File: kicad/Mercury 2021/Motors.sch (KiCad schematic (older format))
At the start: 13 parts

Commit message: Updated new board
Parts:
- removed U? (x4): MDD10A, symbol Mercury:MDD10A
- removed U? (x2): PCA9685, symbol Mercury:PCA9685
- added J22: Conn_02x03_Counter_Clockwise, symbol Connector_Generic:Conn_02x03_Counter_Clockwise
- added J23, J24: Conn_01x02_Female, symbol Connector:Conn_01x02_Female
- added J25: Conn_01x06_Female, symbol Connector:Conn_01x06_Female
- added J26, J27, J29: Conn_01x05_Female, symbol Connector:Conn_01x05_Female
- added J28: Conn_01x03_Female, symbol Connector:Conn_01x03_Female
- added unit 4 of U12
- added unit 5 of U12
- U11, U13: renamed from U?; value MDD10A -> PCA9685; footprint (none) -> Connector_PinHeader_2.54mm:PinHeader_1x05_P2.54mm_Vertical
- U12: renamed from U?; footprint (none) -> Connector_PinHeader_2.54mm:PinHeader_1x06_P2.54mm_Vertical
- gave numbers to parts that had none: 1
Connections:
- net LM_GND: now also U13.1 (B-)
- net RM_GND: now also U11.1 (B-)
- net RM_VIN: now reaches U11.2 (B+)
- net LM_VIN: now reaches U13.2 (B+)
- net Servo_VIN: now reaches U12.1 (V+)
- net Servo_GND: now reaches U12.2 (GND)
- net Pi_3v3: now reaches J15.1 (3V3)
- net Pi_3v3: now also J15.17 (3V3), J26.4 (Pin_4), J26.5 (Pin_5)
- net Pi_GPIO15: now reaches J15.10 (GPIO15/RXD)
- net Pi_GPIO15: now also J23.1 (Pin_1)
- net Pi_GPIO17: now reaches J15.11 (GPIO17)
- net Pi_GPIO17: now also J24.1 (Pin_1)
- net Pi_GPIO27: now reaches J15.13 (GPIO27)
- net Pi_GPIO27: now also J25.1 (Pin_1)
- net Servo_GND_GND: now reaches J15.14 (GND)
- net Pi_GPIO22: now reaches J15.15 (GPIO22)
- net Pi_GPIO22: now also J25.6 (Pin_6)
- net Pi_GPIO23: now reaches J15.16 (GPIO23)
- net Pi_GPIO23: now also J25.5 (Pin_5)
- net Pi_GPIO24: now reaches J15.18 (GPIO24)
- net Pi_GPIO24: now also J25.4 (Pin_4)
- net Pi_GPIO10: now reaches J15.19 (MOSI0/GPIO10)
- net Pi_GPIO10: now also J29.4 (Pin_4)
- net Pi_5v: now reaches J15.2 (5V)
- net Pi_5v: now also J15.4 (5V), J26.1 (Pin_1), J26.2 (Pin_2)
- net Pi_GND: now reaches J15.20 (GND)
- net Pi_GND: now also J15.25 (GND), J15.30 (GND), J15.34 (GND), J15.39 (GND), J27.1 (Pin_1), J27.2 (Pin_2), J27.3 (Pin_3), J27.4 (Pin_4), J27.5 (Pin_5)
- net Pi_GPIO09: now reaches J15.21 (MISO0/GPIO9)
- net Pi_GPIO09: now also J29.3 (Pin_3)
- net Pi_GPIO25: now reaches J15.22 (GPIO25)
- net Pi_GPIO25: now also J25.3 (Pin_3)
- net Pi_GPIO11: now reaches J15.23 (SCLK0/GPIO11)
- net Pi_GPIO11: now also J29.5 (Pin_5)
- net Pi_GPIO08: now reaches J15.24 (~CE0~/GPIO8)
- net Pi_GPIO08: now also J29.2 (Pin_2)
- net Pi_GPIO07: now reaches J15.26 (~CE1~/GPIO7)
- net Pi_GPIO07: now also J29.1 (Pin_1)
- net Pi_GPIO00: now reaches J15.27 (ID_SD/GPIO0)
- net Pi_GPIO00: now also J28.1 (Pin_1)
- net Pi_GPIO01: now reaches J15.28 (ID_SC/GPIO1)
- net Pi_GPIO01: now also J28.2 (Pin_2)
- net Servo_SDA: now reaches J15.3 (SDA/GPIO2)
- net Servo_SDA: now also U12.4 (SDA)
- net Pi_GPIO16: now reaches J15.36 (GPIO16)
- net Pi_GPIO16: now also J24.2 (Pin_2)
- net Pi_GPIO26: now reaches J15.37 (GPIO26)
- net Pi_GPIO26: now also J25.2 (Pin_2)
- net Servo_SCL: now reaches J15.5 (SCL/GPIO3)
- net Servo_SCL: now also U12.3 (SCL)
- net Pi_GPIO04: now reaches J15.7 (GCLK0/GPIO4)
- net Pi_GPIO04: now also J28.3 (Pin_3)
- net Pi_GPIO14: now reaches J15.8 (GPIO14/TXD)
- net Pi_GPIO14: now also J23.2 (Pin_2)
- net Servo_CTL_GND: now reaches U12.1 (GND)
- net Servo_OE: now reaches U12.2 (OE)
- net Serco_VCC: now reaches U12.5 (VCC)
- net Servo_V+: now reaches U12.6 (V+)
- new net: J22.1 (Pin_1), U12.1 (PWM_0)
- new net: J22.2 (Pin_2), U12.2 (V+)
- new net: J22.3 (Pin_3), U12.3 (GND)
- new net: J22.6 (Pin_6), U12.1 (PWM_1)
- new net: J22.5 (Pin_5), U12.2 (V+)
- new net: J22.4 (Pin_4), U12.3 (GND)
- no-connect marks 0 -> 4
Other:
- moved on the sheet: U11C, U12C, U13C

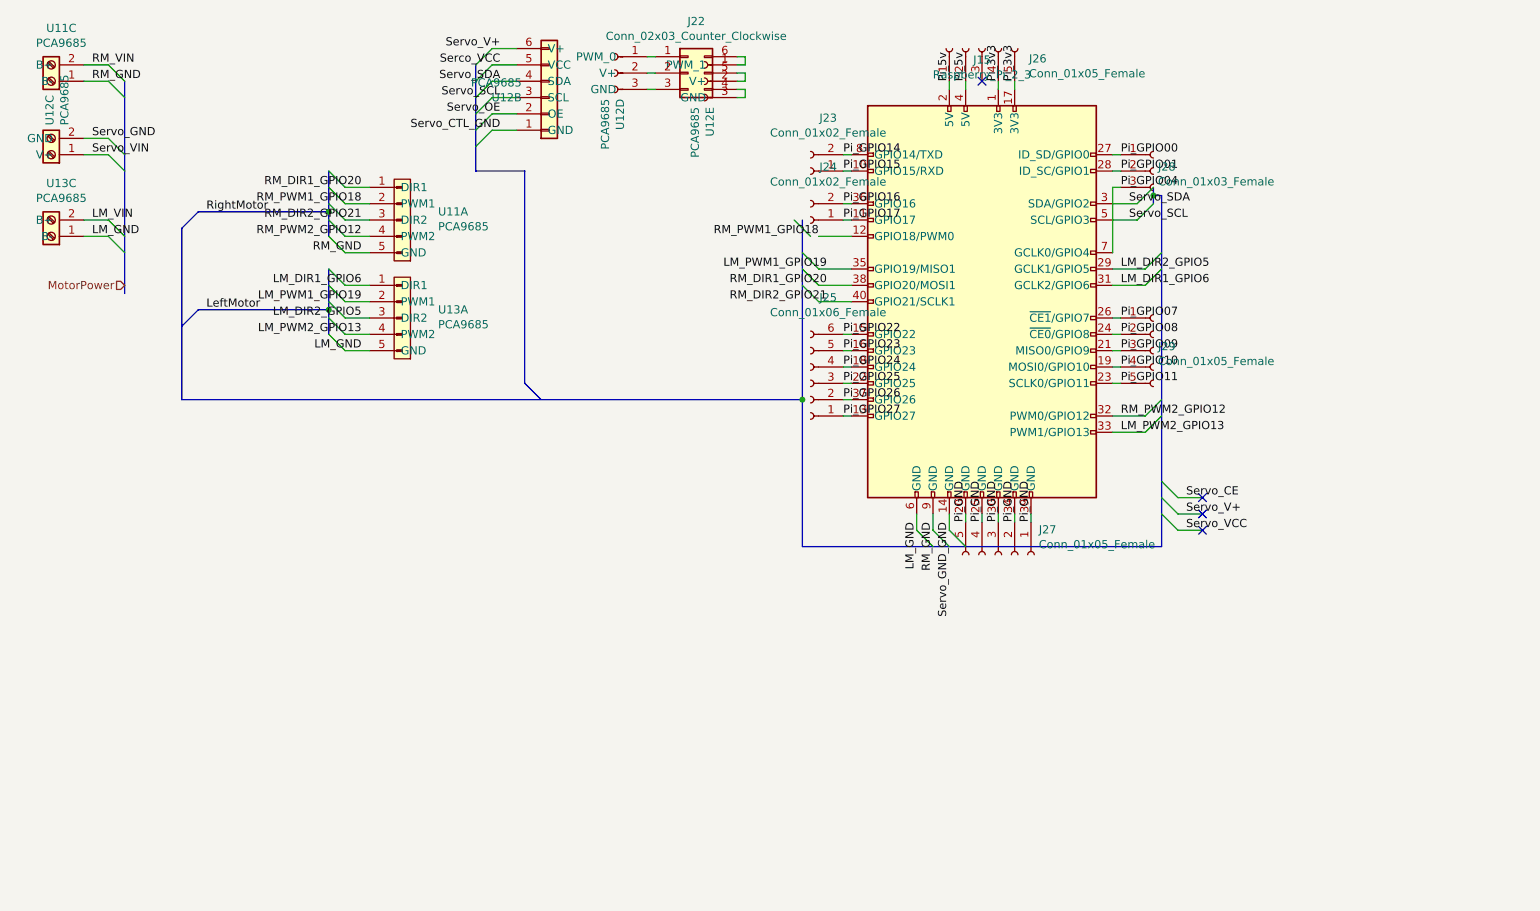
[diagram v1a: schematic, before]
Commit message: Updated the new PCB (lots of notes)
- added net
- changed symbols
- added footprints
- added ability to put the pi -> arduino cable through the board
- fixed global labels
- named connectors
- started adding things to title block

Notes:
- footprints for some parts were chosen at random, connectors need to be chosen on digikey
-- connectors for ribbon cables
-- USB connectors
-- screw terminals
- for these, the footprints may be wrong, so we need to make sure the connectors for them are spaced right
-- arduino
-- servo controller
-- PWM controller
- Board is unorganized, cluttered, and unusable, needs to be managed. considerations:
-- Pins carrying power and data should be separated by distance or GND
-- able to access connectors (not blocked by other things)
- Finish adding things to the title blocks and the PCB silkscreen
-- names or members
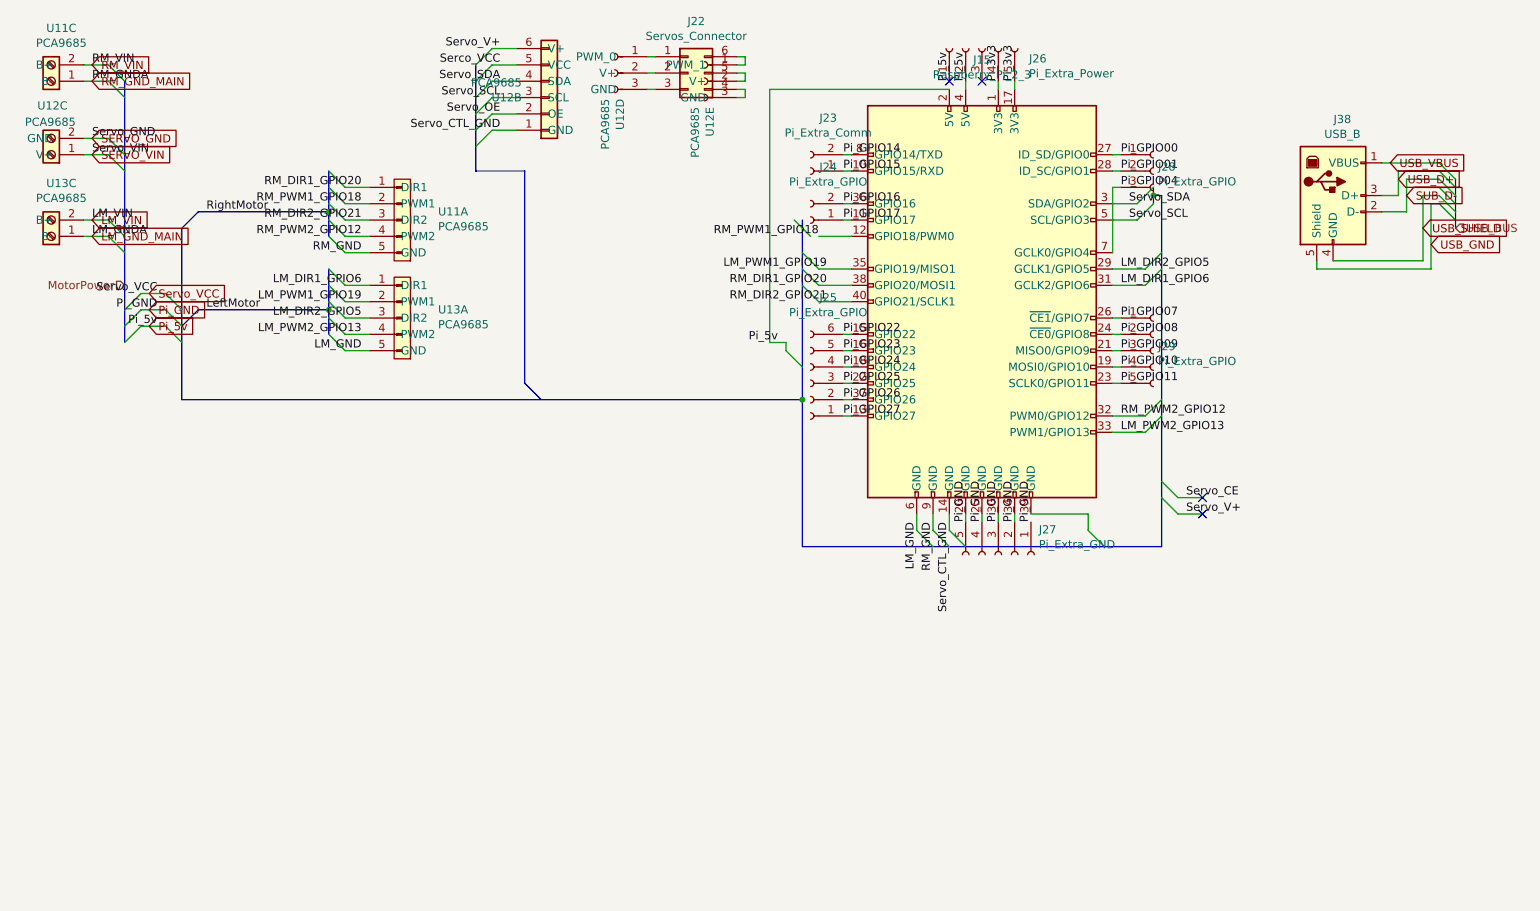
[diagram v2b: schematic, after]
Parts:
- added J38: USB_B, Connector_USB:USB_B_TE_5787834_Vertical, symbol Connector:USB_B
- J15: footprint (none) -> Connector_PinSocket_2.54mm:PinSocket_2x20_P2.54mm_Horizontal
- J22: value Conn_02x03_Counter_Clockwise -> Servos_Connector; footprint (none) -> Connector_PinSocket_2.54mm:PinSocket_2x03_P2.54mm_Vertical
- J23: value Conn_01x02_Female -> Pi_Extra_Comm; footprint (none) -> Connector_PinSocket_2.54mm:PinSocket_1x02_P2.54mm_Vertical
- J24: value Conn_01x02_Female -> Pi_Extra_GPIO; footprint (none) -> Connector_PinSocket_2.54mm:PinSocket_1x02_P2.54mm_Vertical
- J25: value Conn_01x06_Female -> Pi_Extra_GPIO; footprint (none) -> Connector_PinSocket_2.54mm:PinSocket_1x06_P2.54mm_Vertical
- J26: value Conn_01x05_Female -> Pi_Extra_Power; footprint (none) -> Connector_PinSocket_2.54mm:PinSocket_1x05_P2.54mm_Vertical
- J27: value Conn_01x05_Female -> Pi_Extra_GND; footprint (none) -> Connector_PinSocket_2.54mm:PinSocket_1x05_P2.54mm_Vertical
- J28: value Conn_01x03_Female -> Pi_Extra_GPIO; footprint (none) -> Connector_PinSocket_2.54mm:PinSocket_1x03_P2.54mm_Vertical
- J29: value Conn_01x05_Female -> Pi_Extra_GPIO; footprint (none) -> Connector_PinSocket_2.54mm:PinSocket_1x05_P2.54mm_Vertical
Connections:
- net Servo_GND_GND is gone; now on net Servo_CTL_GND: J15.14 (GND)
- net LM_GND: no longer U13.1 (B-)
- net Pi_GND: no longer J15.39 (GND)
- net RM_GND: no longer U11.1 (B-)
- net Servo_GND renamed SERVO_GND
- net Servo_VIN renamed SERVO_VIN
- new net LM_GND_MAIN: U13.1 (B-)
- new net RM_GND_MAIN: U11.1 (B-)
- new net SUB_D-: J38.2 (D-)
- new net USB_D+: J38.3 (D+)
- new net USB_GND: J38.5 (Shield)
- new net USB_SHIELD: J38.4 (GND)
- new net USB_VBUS: J38.1 (VBUS)
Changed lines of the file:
@@
 $Descr A4 11693 8268
 encoding utf-8
-Sheet 3 3
-Title ""
-Date ""
-Rev ""
-Comp ""
+Sheet 2 4
+Title "Mercury 2021 Motherboard"
+Date "2021-04-14"
+Rev "2.0 Alpha"
+Comp "Kansas State University Robotics Competition Team"
 Comment1 ""
 Comment2 ""
 Comment3 ""
-Comment4 ""
+Comment4 "https://github.com/ksurct/mercury2021/issues/10"
 $EndDescr
 $Comp
@@
 F 0 "J15" H 6450 3681 50  0000 C CNN
 F 1 "Raspberry_Pi_2_3" H 6450 3590 50  0000 C CNN
-F 2 "" H 6450 2200 50  0001 C CNN
+F 2 "Connector_PinSocket_2.54mm:PinSocket_2x20_P2.54mm_Horizontal" H 6450 2200 50  0001 C CNN
 F 3 "https://www.raspberrypi.org/documentation/hardware/raspberrypi/schematics/rpi_SCH_3bplus_1p0_reduced.pdf" H 6450 2200 50  0001 C CNN
 	1    6450 2200
@@
 AR Path="/609567C6/6098200C" Ref="U?"  Part="3"
 AR Path="/60979A3C/6098200C" Ref="U12"  Part="3"
-F 0 "U12" H 880 1259 50  0000 L CNN
-F 1 "PCA9685" H 880 1168 50  0000 L CNN
+F 0 "U12" V 1000 1150 50  0000 L CNN
+F 1 "PCA9685" V 900 1100 50  0000 L CNN
 F 2 "Connector_PinHeader_2.54mm:PinHeader_1x06_P2.54mm_Vertical" H 750 1450 50  0001 C CNN
 F 3 "" H 750 1450 50  0001 C CNN
@@
 Servo_CTL_GND
 Text Label 6250 3550 3    50   ~ 0
-Servo_GND_GND
+Servo_CTL_GND
 Text Label 3500 1050 2    50   ~ 0
 Servo_OE
@@
 	7550 3400 7650 3500
 Entry Wire Line
-	7550 3500 7650 3600
-Entry Wire Line
 	7550 3300 7650 3400
 Wire Wire Line
@@
 Wire Wire Line
 	7650 3500 7800 3500
-Wire Wire Line
-	7650 3600 7800 3600
 NoConn ~ 7800 3400
 NoConn ~ 7800 3500
-NoConn ~ 7800 3600
 Text Label 7700 3400 0    50   ~ 0
 Servo_CE
 Text Label 7700 3500 0    50   ~ 0
 Servo_V+
-Text Label 7700 3600 0    50   ~ 0
-Servo_VCC
 Entry Wire Line
 	1100 750  1200 850
@@
 Text Label 1000 750  0    50   ~ 0
 RM_VIN
-Text Label 1000 850  0    50   ~ 0
-RM_GND
 Text Label 1000 1200 0    50   ~ 0
 Servo_GND
@@
 Text Label 1000 1700 0    50   ~ 0
 LM_VIN
-Text Label 1000 1800 0    50   ~ 0
-LM_GND
 Text HLabel 1200 2100 0    50   Input ~ 0
 MotorPower
@@
 P 4650 800
 F 0 "J22" H 4700 1117 50  0000 C CNN
-F 1 "Conn_02x03_Counter_Clockwise" H 4700 1026 50  0000 C CNN
-F 2 "" H 4650 800 50  0001 C CNN
+F 1 "Servos_Connector" H 4700 1026 50  0000 C CNN
+F 2 "Connector_PinSocket_2.54mm:PinSocket_2x03_P2.54mm_Vertical" H 4650 800 50  0001 C CNN
 F 3 "~" H 4650 800 50  0001 C CNN
 	1    4650 800
@@
 P 5400 2700
 F 0 "J25" H 5292 2175 50  0000 C CNN
-F 1 "Conn_01x06_Female" H 5292 2266 50  0000 C CNN
-F 2 "" H 5400 2700 50  0001 C CNN
+F 1 "Pi_Extra_GPIO" H 5292 2266 50  0000 C CNN
+F 2 "Connector_PinSocket_2.54mm:PinSocket_1x06_P2.54mm_Vertical" H 5400 2700 50  0001 C CNN
 F 3 "~" H 5400 2700 50  0001 C CNN
 	1    5400 2700
@@
 P 5400 1700
 F 0 "J24" H 5292 1375 50  0000 C CNN
-F 1 "Conn_01x02_Female" H 5292 1466 50  0000 C CNN
-F 2 "" H 5400 1700 50  0001 C CNN
+F 1 "Pi_Extra_GPIO" H 5292 1466 50  0000 C CNN
+F 2 "Connector_PinSocket_2.54mm:PinSocket_1x02_P2.54mm_Vertical" H 5400 1700 50  0001 C CNN
 F 3 "~" H 5400 1700 50  0001 C CNN
 	1    5400 1700
@@
 P 5400 1400
 F 0 "J23" H 5292 1075 50  0000 C CNN
-F 1 "Conn_01x02_Female" H 5292 1166 50  0000 C CNN
-F 2 "" H 5400 1400 50  0001 C CNN
+F 1 "Pi_Extra_Comm" H 5292 1166 50  0000 C CNN
+F 2 "Connector_PinSocket_2.54mm:PinSocket_1x02_P2.54mm_Vertical" H 5400 1400 50  0001 C CNN
 F 3 "~" H 5400 1400 50  0001 C CNN
 	1    5400 1400
@@
 P 7500 2500
 F 0 "J29" H 7528 2526 50  0000 L CNN
-F 1 "Conn_01x05_Female" H 7528 2435 50  0000 L CNN
-F 2 "" H 7500 2500 50  0001 C CNN
+F 1 "Pi_Extra_GPIO" H 7528 2435 50  0000 L CNN
+F 2 "Connector_PinSocket_2.54mm:PinSocket_1x05_P2.54mm_Vertical" H 7500 2500 50  0001 C CNN
 F 3 "~" H 7500 2500 50  0001 C CNN
 	1    7500 2500
@@
 P 6550 3750
 F 0 "J27" V 6396 3998 50  0000 L CNN
-F 1 "Conn_01x05_Female" V 6487 3998 50  0000 L CNN
-F 2 "" H 6550 3750 50  0001 C CNN
+F 1 "Pi_Extra_GND" V 6487 3998 50  0000 L CNN
+F 2 "Connector_PinSocket_2.54mm:PinSocket_1x05_P2.54mm_Vertical" H 6550 3750 50  0001 C CNN
 F 3 "~" H 6550 3750 50  0001 C CNN
 	1    6550 3750
@@
 P 6450 650
 F 0 "J26" V 6388 362 50  0000 R CNN
-F 1 "Conn_01x05_Female" V 6297 362 50  0000 R CNN
-F 2 "" H 6450 650 50  0001 C CNN
+F 1 "Pi_Extra_Power" V 6297 362 50  0000 R CNN
+F 2 "Connector_PinSocket_2.54mm:PinSocket_1x05_P2.54mm_Vertical" H 6450 650 50  0001 C CNN
 F 3 "~" H 6450 650 50  0001 C CNN
 	1    6450 650
@@
 P 7500 1400
 F 0 "J28" H 7528 1426 50  0000 L CNN
-F 1 "Conn_01x03_Female" H 7528 1335 50  0000 L CNN
-F 2 "" H 7500 1400 50  0001 C CNN
+F 1 "Pi_Extra_GPIO" H 7528 1335 50  0000 L CNN
+F 2 "Connector_PinSocket_2.54mm:PinSocket_1x03_P2.54mm_Vertical" H 7500 1400 50  0001 C CNN
 F 3 "~" H 7500 1400 50  0001 C CNN
 	1    7500 1400
@@
 	7300 2700 7250 2700
 Wire Wire Line
-	6750 3550 6750 3500
-Wire Wire Line
 	6650 3500 6650 3550
 Wire Wire Line
@@
 	6350 850  6350 900
 Wire Wire Line
-	6250 850  6250 900
-Wire Wire Line
 	5000 700  4950 700
 Wire Wire Line
@@
 Wire Wire Line
 	5000 950  4950 950
+Text Label 1000 850  0    50   ~ 0
+RM_GNDA
+Text Label 1000 1800 0    50   ~ 0
+LM_GNDA
+Text GLabel 1000 750  2    50   Input ~ 0
+RM_VIN
+Text GLabel 1000 850  2    50   Input ~ 0
+RM_GND_MAIN
+Text GLabel 1000 1200 2    50   Input ~ 0
+SERVO_GND
+Text GLabel 1000 1300 2    50   Input ~ 0
+SERVO_VIN
+Text GLabel 1000 1700 2    50   Input ~ 0
+LM_VIN
+Text GLabel 1000 1800 2    50   Input ~ 0
+LM_GND_MAIN
+Entry Wire Line
+	1550 2250 1450 2150
+Text Label 1400 2150 2    50   ~ 0
+Servo_VCC
+Entry Wire Line
+	1300 2150 1200 2250
+Wire Wire Line
+	1300 2150 1450 2150
+NoConn ~ 6250 850
+Wire Wire Line
+	6250 900  5150 900
+Wire Wire Line
+	5150 900  5150 2450
+Entry Wire Line
+	5250 2500 5350 2600
+Wire Wire Line
+	5150 2450 5250 2450
+Wire Wire Line
+	5250 2450 5250 2500
+Text Label 5200 2450 2    50   ~ 0
+Pi_5v
+Wire Wire Line
+	6750 3500 7100 3500
+Wire Wire Line
+	7100 3500 7100 3600
+Entry Wire Line
+	7100 3600 7200 3700
+Entry Wire Line
+	1550 2350 1450 2250
+Entry Wire Line
+	1300 2250 1200 2350
+Entry Wire Line
+	1550 2450 1450 2350
+Text Label 1400 2350 2    50   ~ 0
+Pi_5v
+Entry Wire Line
+	1300 2350 1200 2450
+Wire Wire Line
+	1300 2350 1450 2350
+Wire Wire Line
+	1300 2250 1450 2250
+Text Label 1400 2250 2    50   ~ 0
+Pi_GND
+Text GLabel 1350 2150 2    50   Input ~ 0
+Servo_VCC
+Text GLabel 1350 2250 2    50   Input ~ 0
+Pi_GND
+Text GLabel 1350 2350 2    50   Input ~ 0
+Pi_5v
+Wire Wire Line
+	8900 1550 9000 1550
+Wire Wire Line
+	9000 1550 9000 1400
+Wire Wire Line
+	8900 1650 9050 1650
+Wire Wire Line
+	9050 1650 9050 1450
+Wire Wire Line
+	8600 1950 9150 1950
+Wire Wire Line
+	9150 1950 9150 1550
+Wire Wire Line
+	8500 1950 8500 2000
+Wire Wire Line
+	8500 2000 9200 2000
+Wire Wire Line
+	9200 2000 9200 1600
+Wire Wire Line
+	9200 1600 9250 1600
+Wire Wire Line
+	9150 1550 9250 1550
+Wire Wire Line
+	9100 1500 9250 1500
+Wire Wire Line
+	9050 1450 9250 1450
+Wire Wire Line
+	9000 1400 9250 1400
+Wire Wire Line
+	8900 1350 9250 1350
+Entry Wire Line
+	9250 1350 9350 1450
+Entry Wire Line
+	9250 1400 9350 1500
+Entry Wire Line
+	9250 1450 9350 1550
+Entry Wire Line
+	9250 1500 9350 1600
+Entry Wire Line
+	9250 1550 9350 1650
+Entry Wire Line
+	9250 1600 9350 1700
+Wire Bus Line
+	2450 2250 2450 2400
+Wire Bus Line
+	2450 1650 2450 1800
 Wire Bus Line
 	1550 2800 5350 2800
 Wire Bus Line
+	2450 1400 2450 1650
+Wire Bus Line
+	2450 2000 2450 2250
+Wire Bus Line
+	5350 3700 7550 3700
+Wire Bus Line
+	5350 1700 5350 2800
+Wire Bus Line
 	1550 1750 1550 2800
 Wire Bus Line
-	2450 2250 2450 2400
-Wire Bus Line
-	2450 1650 2450 1800
-Wire Bus Line
-	2450 1400 2450 1650
-Wire Bus Line
-	2450 2000 2450 2250
-Wire Bus Line
-	5350 3700 7550 3700
-Wire Bus Line
-	5350 1700 5350 2800
+	9350 1450 9350 1750
 Wire Bus Line
 	3350 750  3350 1400
@@
 	7550 1550 7550 3700
 Wire Bus Line
-	1200 850  1200 2150
+	1200 850  1200 2450
+Text HLabel 9350 1750 2    50   Input ~ 0
+USB_BUS
+Text GLabel 8950 1350 2    50   Input ~ 0
+USB_VBUS
+Text GLabel 9000 1450 2    50   Input ~ 0
+USB_D+
+Text GLabel 9050 1550 2    50   Input ~ 0
+SUB_D-
+Text GLabel 9150 1750 2    50   Input ~ 0
+USB_SHIELD
+Text GLabel 9200 1850 2    50   Input ~ 0
+USB_GND
+$Comp
+L Connector:USB_B J38
+U 1 1 612E76FA
+P 8600 1550
+F 0 "J38" H 8657 2017 50  0000 C CNN
+F 1 "USB_B" H 8657 1926 50  0000 C CNN
+F 2 "Connector_USB:USB_B_TE_5787834_Vertical" H 8750 1500 50  0001 C CNN
+F 3 " ~" H 8750 1500 50  0001 C CNN
+	1    8600 1550
+	1    0    0    -1
+$EndComp
 $EndSCHEMATC
